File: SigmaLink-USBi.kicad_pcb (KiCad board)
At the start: 2 copper layers, 64 x 39 mm, 40 parts, among them J1 USB_C_Receptacle_USB2.0, J2 Program, J3 Target, U1 LM1117-3.3, U2 74LVC2G66, U3 TPS2051B, U4 24LC512, U5 MAX809, U6 CY7C68013A-56, Y1 24MHz

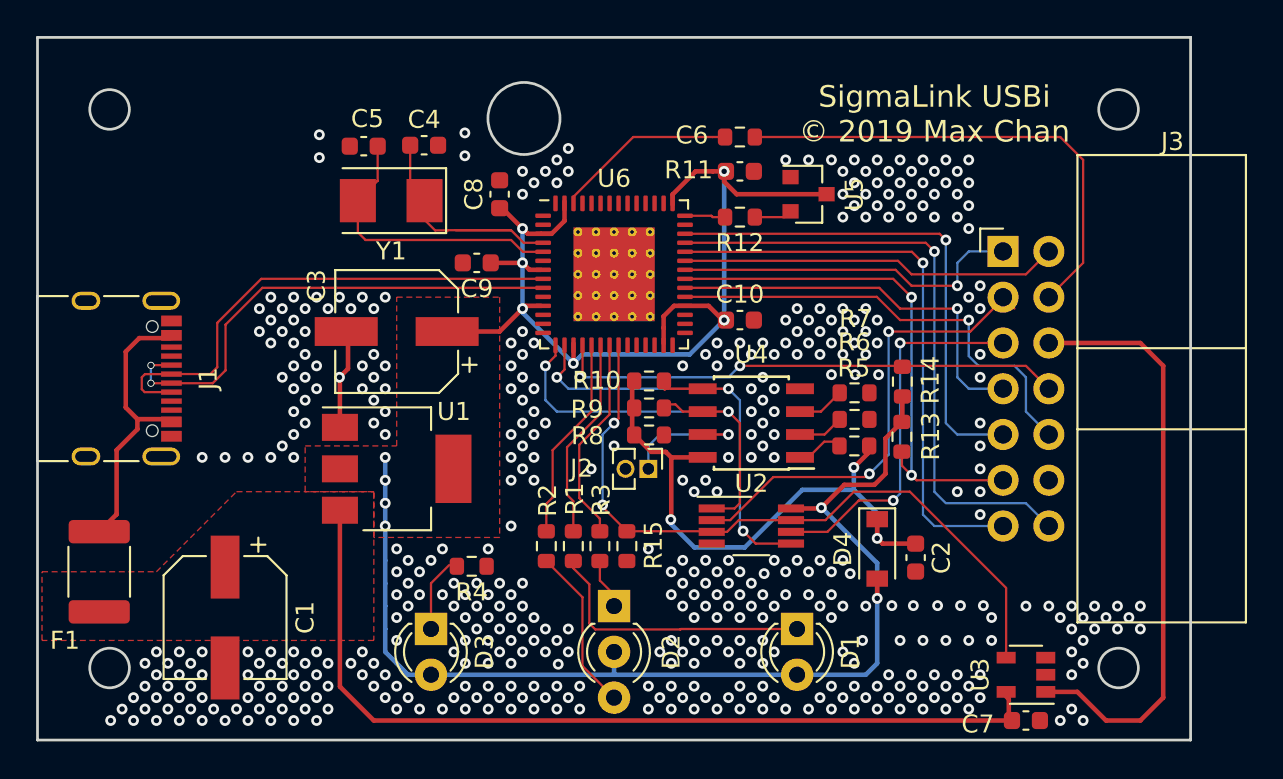
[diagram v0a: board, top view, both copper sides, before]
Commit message: 修改丝印
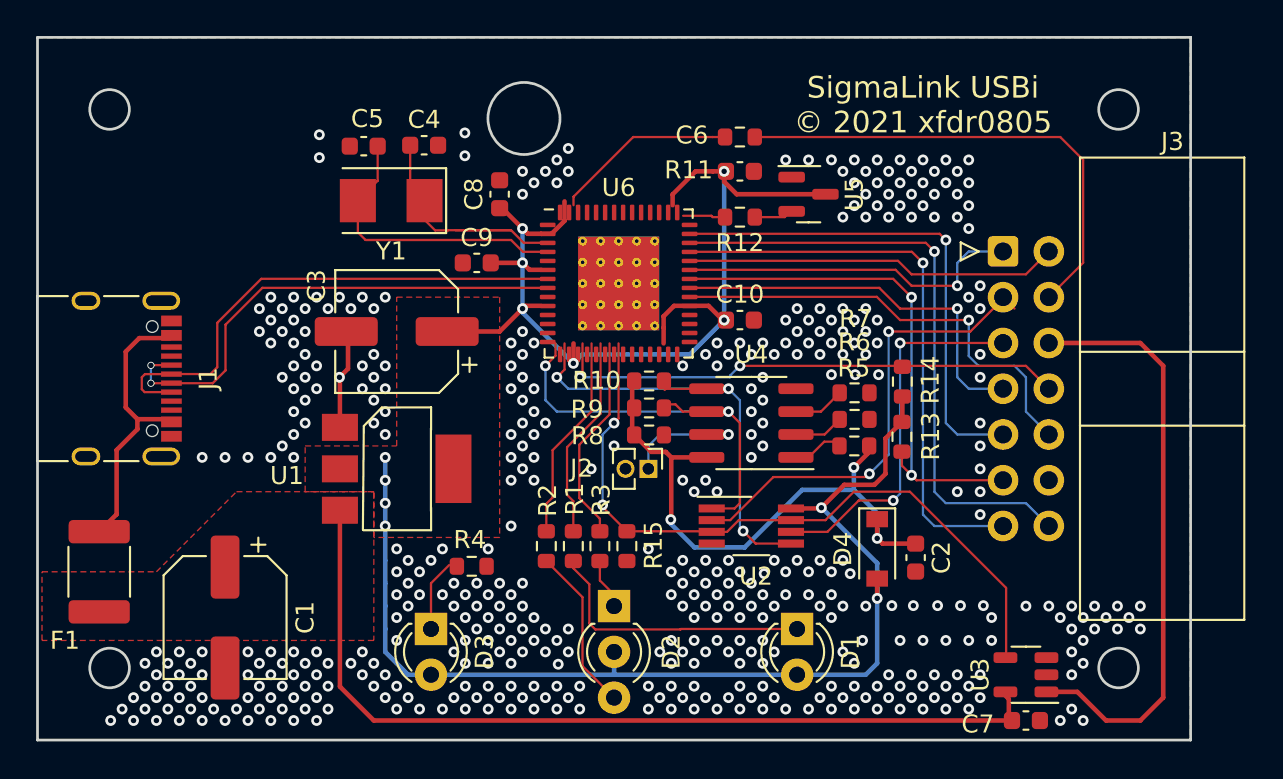
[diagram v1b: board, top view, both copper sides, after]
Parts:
- moved U6 0.57 mm to (150.3, 94.2)
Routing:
- net GND: vias 455 -> 449
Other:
- board text added: "SigmaLink USBi © 2021 xfdr0805"
- board text removed: "SigmaLink USBi © 2019 Max Chan"
